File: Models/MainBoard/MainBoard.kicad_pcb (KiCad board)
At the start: 4 copper layers, 54.6 x 62.4 mm, 9 parts, among them J1 PinSocket_1x24, J2 PinSocket_1x24, M1 DowelPin_2.5mm, M2 DowelPin_2.5mm, U1 SOIC-16-Wide, U2 SOIC-16-Wide

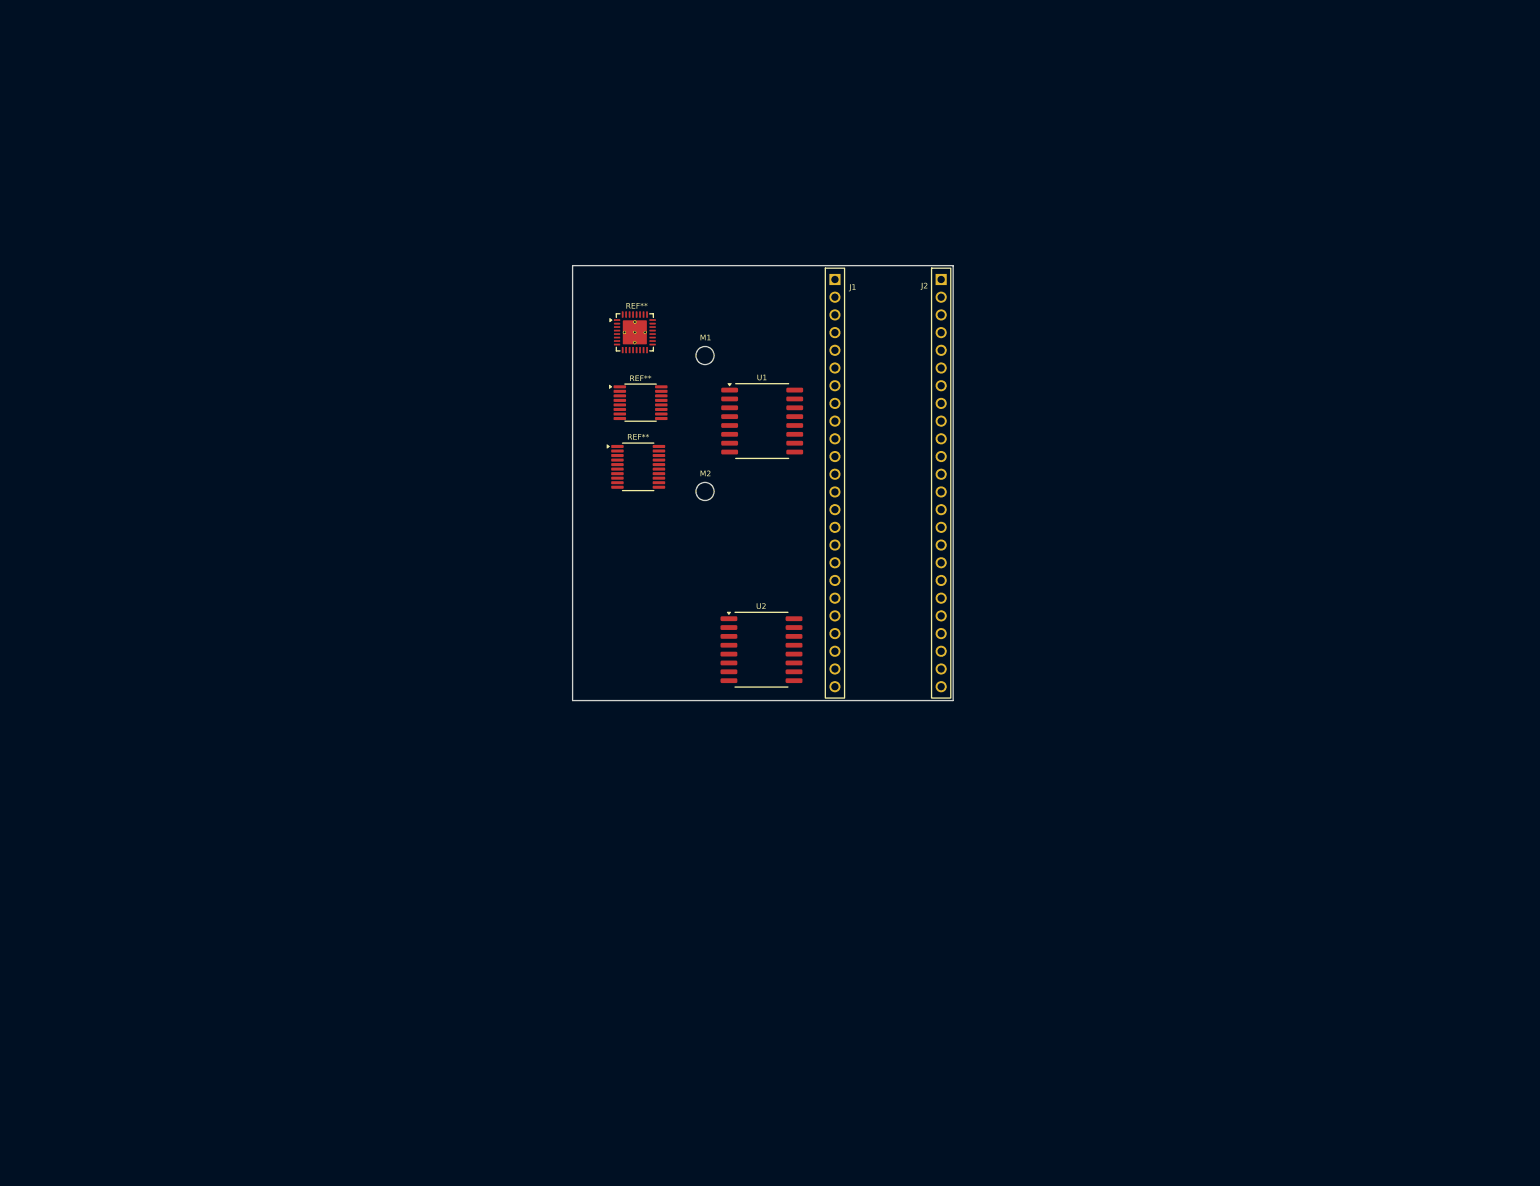
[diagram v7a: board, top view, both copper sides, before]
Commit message: This is not an acceptable connector packing arrangement
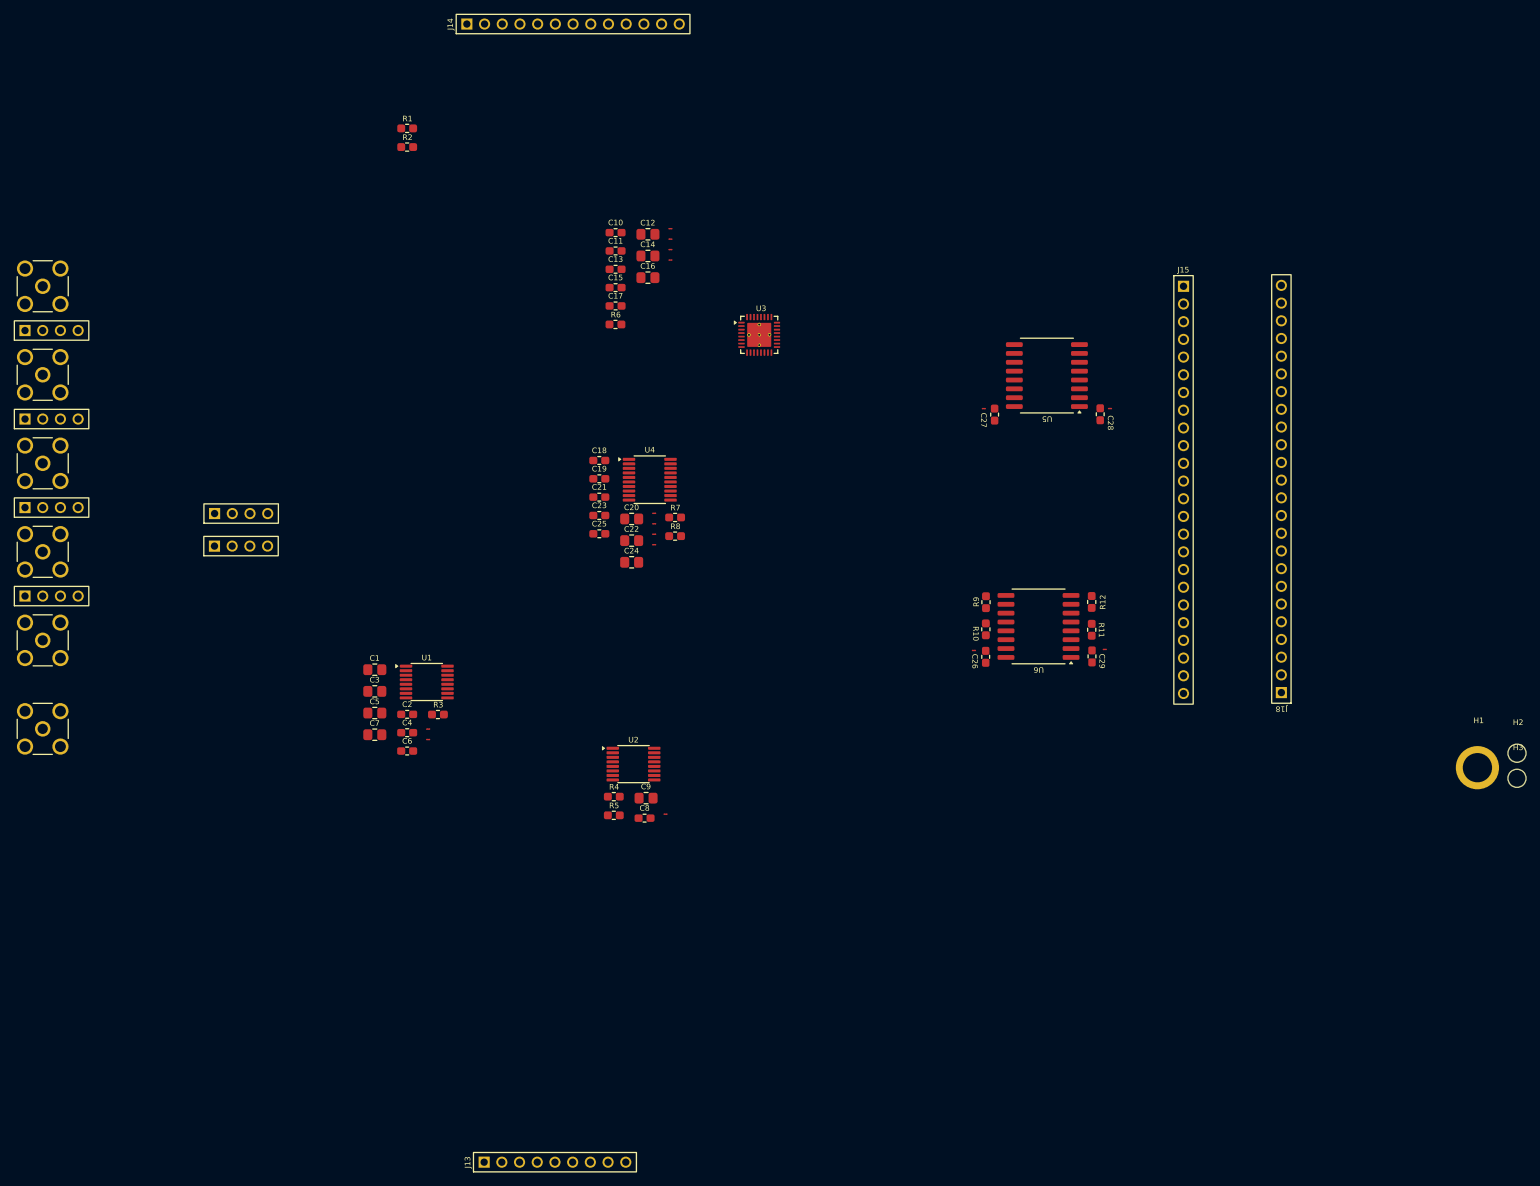
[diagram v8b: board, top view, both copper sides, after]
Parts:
- removed M1, M2: DowelPin_2.5mm, Connector_Custom:DowelPin_2.5mm
- removed REF**: TSSOP-20, IC:TSSOP-20
- removed REF**: TSSOP-16, IC:TSSOP-16
- removed REF**: VQFN-32, IC:VQFN-32
- added C1: 10 uF, 0805, TwoTerminal:CAPC0805, F.Cu at (101.6, 115.7)
- added C10: 220 nF, 0603, TwoTerminal:CAPC0603, F.Cu at (136.2, 53.0)
- added C11: 100 nF, 0603, TwoTerminal:CAPC0603, F.Cu at (136.2, 55.6)
- added C12: 10 uF, 0805, TwoTerminal:CAPC0805, F.Cu at (140.8, 53.2)
- added C13: 100 nF, 0603, TwoTerminal:CAPC0603, F.Cu at (136.2, 58.2)
- added C14: 10 uF, 0805, TwoTerminal:CAPC0805, F.Cu at (140.8, 56.3)
- added C15: 100 nF, 0603, TwoTerminal:CAPC0603, F.Cu at (136.2, 60.9)
- added C16: 10 uF, 0805, TwoTerminal:CAPC0805, F.Cu at (140.8, 59.4)
- added C17: 100 nF, 0603, TwoTerminal:CAPC0603, F.Cu at (136.2, 63.5)
- added C18: 220 nF, 0603, TwoTerminal:CAPC0603, F.Cu at (133.8, 85.7)
- added C19: 100 nF, 0603, TwoTerminal:CAPC0603, F.Cu at (133.8, 88.3)
- added C2: 1 uF, 0603, TwoTerminal:CAPC0603, F.Cu at (106.3, 122.1)
- added C20: 10 uF, 0805, TwoTerminal:CAPC0805, F.Cu at (138.5, 94.0)
- added C21: 100 nF, 0603, TwoTerminal:CAPC0603, F.Cu at (133.8, 90.9)
- added C22: 10 uF, 0805, TwoTerminal:CAPC0805, F.Cu at (138.5, 97.2)
- added C23: 100 nF, 0603, TwoTerminal:CAPC0603, F.Cu at (133.8, 93.5)
- added C24: 10 uF, 0805, TwoTerminal:CAPC0805, F.Cu at (138.5, 100.3)
- added C25: 100 nF, 0603, TwoTerminal:CAPC0603, F.Cu at (133.8, 96.2)
- added C26: 100 nF, 0603, TwoTerminal:CAPC0603, F.Cu at (189.3, 113.8)
- added C27: 100 nF, 0603, TwoTerminal:CAPC0603, F.Cu at (190.6, 79.1)
- added C28: 100 nF, 0603, TwoTerminal:CAPC0603, F.Cu at (205.7, 79.0)
- added C29: 100 nF, 0603, TwoTerminal:CAPC0603, F.Cu at (204.5, 113.8)
- added C3: 10 uF, 0805, TwoTerminal:CAPC0805, F.Cu at (101.6, 118.8)
- added C4: 1 uF, 0603, TwoTerminal:CAPC0603, F.Cu at (106.3, 124.7)
- added C5: 10 uF, 0805, TwoTerminal:CAPC0805, F.Cu at (101.6, 121.9)
- added C6: 1 uF, 0603, TwoTerminal:CAPC0603, F.Cu at (106.3, 127.3)
- added C7: 10 uF, 0805, TwoTerminal:CAPC0805, F.Cu at (101.6, 125.0)
- added C8: 100 nF, 0603, TwoTerminal:CAPC0603, F.Cu at (140.3, 137.0)
- added C9: 10 uF, 0805, TwoTerminal:CAPC0805, F.Cu at (140.5, 134.1)
- added H1: Mounting Hole, M2.5, Connector_Custom:Keystone_24929, F.Cu at (259.8, 129.7)
- added H2: Dowel Pin, M2.5, Connector_Custom:DowelPin_2.5mm, F.Cu at (265.5, 127.7)
- added H3: Dowel Pin, M2.5, Connector_Custom:DowelPin_2.5mm, F.Cu at (265.5, 131.3)
- added J10: Conn_01x04_Pin, Connector_Custom:PinConnector_1x4, F.Cu at (55.2, 105.1)
- added J11: Conn_01x04_Pin, Connector_Custom:PinConnector_1x4, F.Cu at (82.5, 93.3)
- added J12: Conn_01x04_Pin, Connector_Custom:PinConnector_1x4, F.Cu at (82.4, 97.9)
- added J13: Conn_01x09_Pin, Connector_Custom:PinConnector_1x9, F.Cu at (127.5, 186.3)
- added J14: Conn_01x13_Pin, Connector_Custom:PinConnector_1x13, F.Cu at (130.1, 23.0)
- added J15: Conn_01x24_Socket, Connector_Custom:PinConnector_1x24, F.Cu at (217.7, 89.9)
- added J18: Conn_01x24_Socket, Connector_Custom:PinConnector_1x24, F.Cu at (231.7, 89.7)
- added J3: Conn_Coaxial, Connector_Custom:RFPC-SMA27-F, F.Cu at (54.0, 86.1)
- added J4: Conn_Coaxial, Connector_Custom:RFPC-SMA27-F, F.Cu at (54.0, 98.8)
- added J5: Conn_Coaxial, Connector_Custom:RFPC-SMA27-F, F.Cu at (54.0, 111.5)
- added J6: Conn_Coaxial, Connector_Custom:RFPC-SMA27-F, F.Cu at (54.0, 124.2)
- added J7: Conn_01x04_Pin, Connector_Custom:PinConnector_1x4, F.Cu at (55.2, 67.0)
- added J8: Conn_01x04_Pin, Connector_Custom:PinConnector_1x4, F.Cu at (55.2, 79.7)
- added J9: Conn_01x04_Pin, Connector_Custom:PinConnector_1x4, F.Cu at (55.2, 92.4)
- added NT1: NetTie_2, Connector_Custom:NetTie_0.2mm, F.Cu at (109.3, 124.2)
- added NT10: NetTie_2, Connector_Custom:NetTie_0.2mm, F.Cu at (141.7, 96.2)
- added NT11: NetTie_2, Connector_Custom:NetTie_0.2mm, F.Cu at (141.7, 97.7)
- added NT12: NetTie_2, Connector_Custom:NetTie_0.2mm, F.Cu at (187.6, 112.9)
- added NT13: NetTie_2, Connector_Custom:NetTie_0.2mm, F.Cu at (189.0, 78.2)
- added NT14: NetTie_2, Connector_Custom:NetTie_0.2mm, F.Cu at (207.1, 78.2)
- added NT15: NetTie_2, Connector_Custom:NetTie_0.2mm, F.Cu at (206.3, 112.8)
- added NT2: NetTie_2, Connector_Custom:NetTie_0.2mm, F.Cu at (109.3, 125.7)
- added NT3: NetTie_2, Connector_Custom:NetTie_0.2mm, F.Cu at (143.3, 136.4)
- added NT4: NetTie_2, Connector_Custom:NetTie_0.2mm, F.Cu at (144.0, 52.4)
- added NT5: NetTie_2, Connector_Custom:NetTie_0.2mm, F.Cu at (144.0, 53.9)
- added NT6: NetTie_2, Connector_Custom:NetTie_0.2mm, F.Cu at (144.0, 55.4)
- added NT7: NetTie_2, Connector_Custom:NetTie_0.2mm, F.Cu at (144.0, 56.9)
- added NT8: NetTie_2, Connector_Custom:NetTie_0.2mm, F.Cu at (141.7, 93.2)
- added NT9: NetTie_2, Connector_Custom:NetTie_0.2mm, F.Cu at (141.7, 94.7)
- added R1: 10, 1%, TwoTerminal:RESC0603, F.Cu at (106.3, 38.0)
- added R10: 10k, 1%, TwoTerminal:RESC0603, F.Cu at (189.3, 109.9)
- added R11: 10k, 1%, TwoTerminal:RESC0603, F.Cu at (204.5, 109.9)
- added R12: 10k, 1%, TwoTerminal:RESC0603, F.Cu at (204.5, 106.0)
- added R2: 10, 1%, TwoTerminal:RESC0603, F.Cu at (106.3, 40.7)
- added R3: 10k, 1%, TwoTerminal:RESC0603, F.Cu at (110.7, 122.1)
- added R4: 10k, 1%, TwoTerminal:RESC0603, F.Cu at (135.9, 133.9)
- added R5: 10k, 1%, TwoTerminal:RESC0603, F.Cu at (135.9, 136.6)
- added R6: 10k, 1%, TwoTerminal:RESC0603, F.Cu at (136.2, 66.1)
- added R7: 4.7k, 1%, TwoTerminal:RESC0603, F.Cu at (144.7, 93.8)
- added R8: 10k, 1%, TwoTerminal:RESC0603, F.Cu at (144.7, 96.5)
- added R9: 10k, 1%, TwoTerminal:RESC0603, F.Cu at (189.3, 106.0)
- added U3: DAC81404, IC:VQFN-32, F.Cu at (156.8, 67.6)
- added U4: DAC81401, IC:TSSOP-20, F.Cu at (141.1, 88.4)
- added U5: ISO7761DW, IC:SOIC-16-Wide, F.Cu at (198.1, 73.5)
- added U6: ISO1641DW, IC:SOIC-16-Wide, F.Cu at (196.8, 109.5)
- J1, J2: value PinSocket_1x24 -> Conn_Coaxial; footprint Connector_Custom:PinSocket_1x24 -> Connector_Custom:RFPC-SMA27-F
- U1: value SOIC-16-Wide -> ADS8699; footprint IC:SOIC-16-Wide -> IC:TSSOP-16
- U2: value SOIC-16-Wide -> AD7745; footprint IC:SOIC-16-Wide -> IC:TSSOP-16
- moved J2 129.8 mm to (54.0, 73.4)
- moved J1 117.1 mm to (54.0, 60.7)
- moved U1 61.0 mm to (109.1, 117.4)
- moved U2 24.6 mm to (138.7, 129.2)
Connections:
- J1 pad 1: (no net) -> /BIAS_OUT
- J1 pad 2: (no net) -> GND
- J2 pad 1: (no net) -> /BIAS_GND
- J2 pad 2: (no net) -> GND
- U1 pad 1: (no net) -> GND
- U1 pad 10: (no net) -> /ADC/MOSI
- U1 pad 11: (no net) -> /CS3
- U1 pad 12: (no net) -> /ADC/SCK
- U1 pad 13: (no net) -> /ADC/MISO
- U1 pad 14: (no net) -> unconnected-(U1-ALARM/SDO-1/GPO-Pad14)
- U1 pad 15: (no net) -> unconnected-(U1-RVS-Pad15)
- U1 pad 16: (no net) -> /ADC/DVDD
- U1 pad 2: (no net) -> /ADC/AVDD
- U1 pad 3: (no net) -> GND
- U1 pad 4: (no net) -> Net-(U1-REFIO)
- U1 pad 5: (no net) -> GND
- U1 pad 6: (no net) -> /ADC/REFCAP
- U1 pad 7: (no net) -> /ADC_IN
- U1 pad 8: (no net) -> /ADC_GND
- U1 pad 9: (no net) -> Net-(U1-*RST)
- U2 pad 1: (no net) -> /CDC/SCL
- U2 pad 10: (no net) -> unconnected-(U2-NC-Pad10)
- U2 pad 11: (no net) -> unconnected-(U2-VIN+-Pad11)
- U2 pad 12: (no net) -> unconnected-(U2-VIN--Pad12)
- U2 pad 13: (no net) -> GND
- U2 pad 14: (no net) -> /CDC/VDD
- U2 pad 15: (no net) -> unconnected-(U2-NC-Pad15)
- U2 pad 16: (no net) -> /CDC/SDA
- U2 pad 2: (no net) -> unconnected-(U2-RDY_N-Pad2)
- U2 pad 3: (no net) -> /CDC_EXC
- U2 pad 4: (no net) -> unconnected-(U2-EXCB-Pad4)
- U2 pad 5: (no net) -> unconnected-(U2-REFIN+-Pad5)
- U2 pad 6: (no net) -> unconnected-(U2-REFIN--Pad6)
- U2 pad 7: (no net) -> unconnected-(U2-CIN1--Pad7)
- U2 pad 8: (no net) -> /CDC_CIN
- U2 pad 9: (no net) -> unconnected-(U2-NC-Pad9)
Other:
- board outline removed
